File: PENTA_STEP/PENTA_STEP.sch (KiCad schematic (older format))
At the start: 154 parts, among them J1 DB25_Female_LCNC, J10 ENC_HEADER, J11 ENC_HEADER, J12 PSoC_PROG, J14 SCREW TERM, J15 SCREW TERM, J16 ENC_HEADER, J17 ENC_HEADER, J18 SCREW TERM, J19 SCREW TERM, J2 MTA-100, J20 CYP_I2C, J3 USB_B, J4 SPARE_IN, J5 ENC_HEADER, J6 Conn_02x02_Odd_Even, J7 CYP_GPIO, J8 ICSP, J9 SCREW TERM, U1 ATTINY841-SSU, U2 CY8C5468AXI-LP106, Y1 10MHz

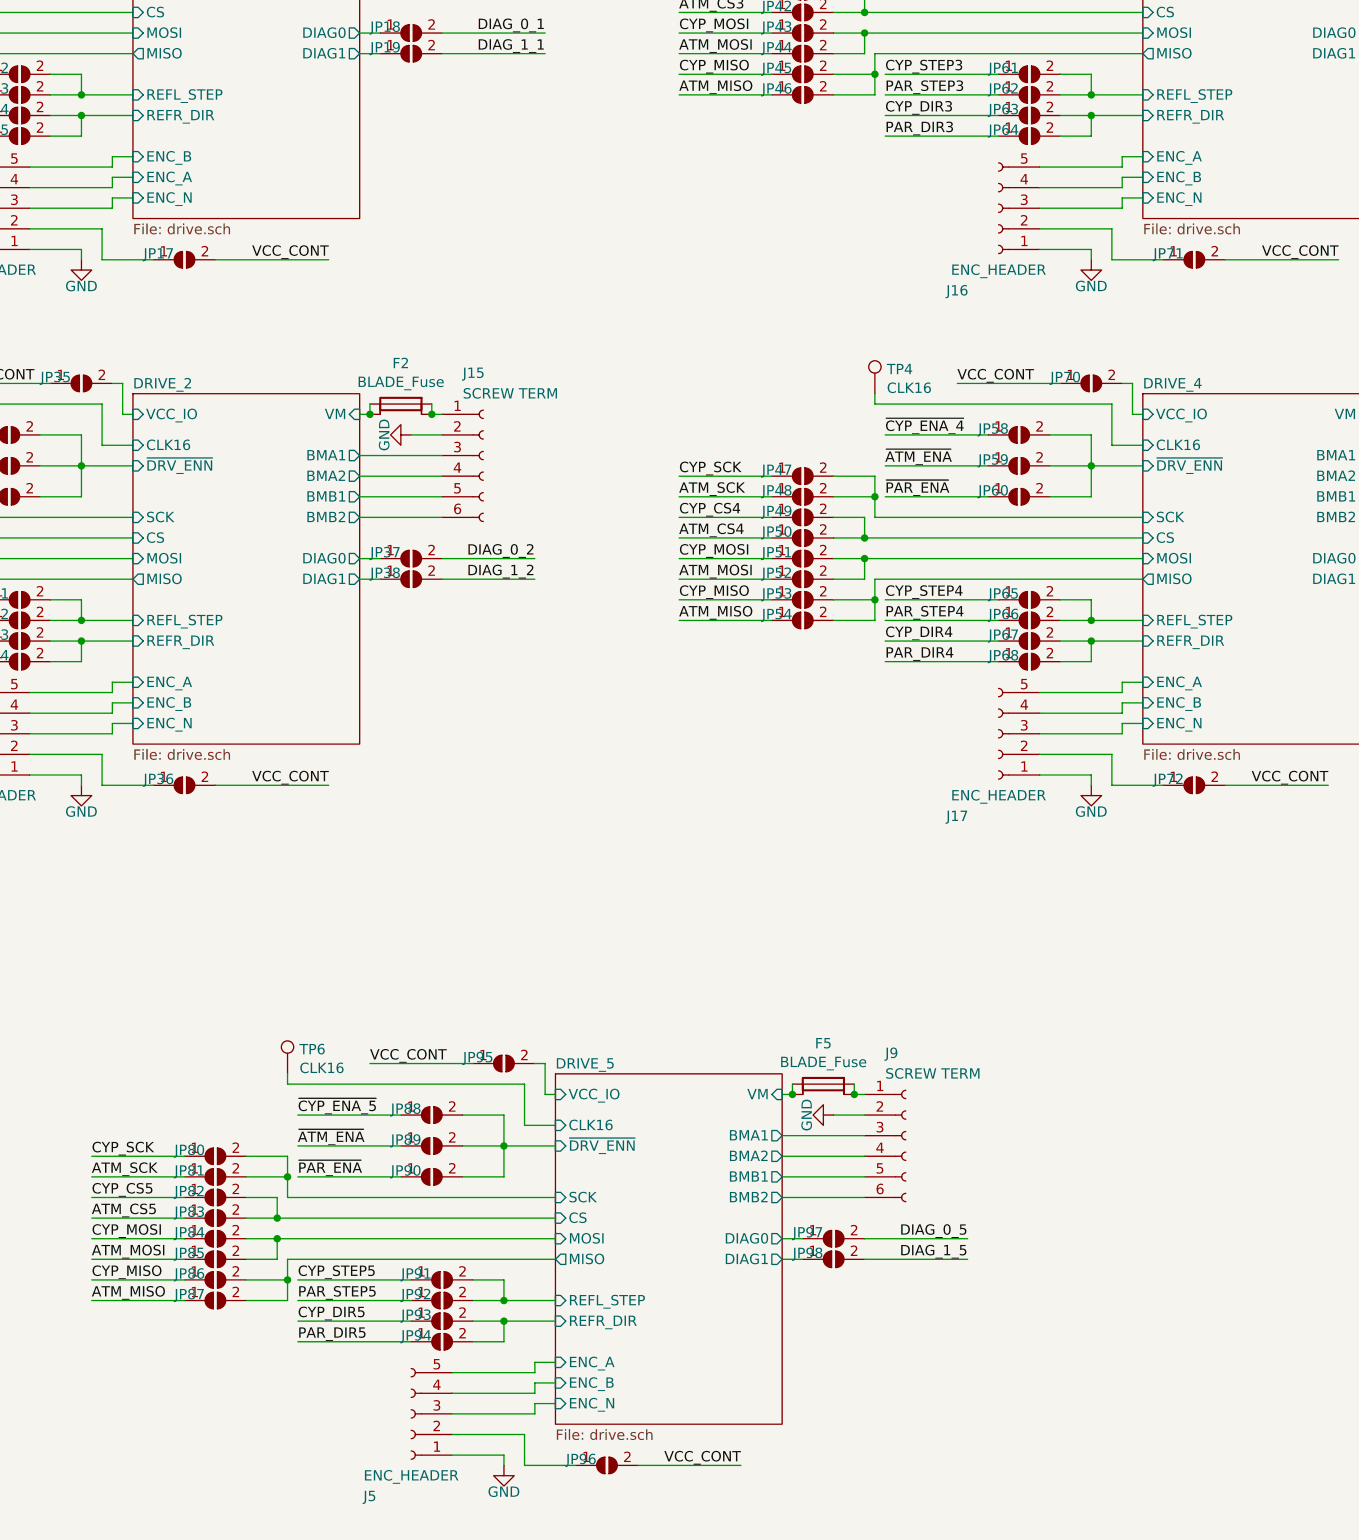
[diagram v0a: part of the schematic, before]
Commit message: corrected symbol and footprint paths
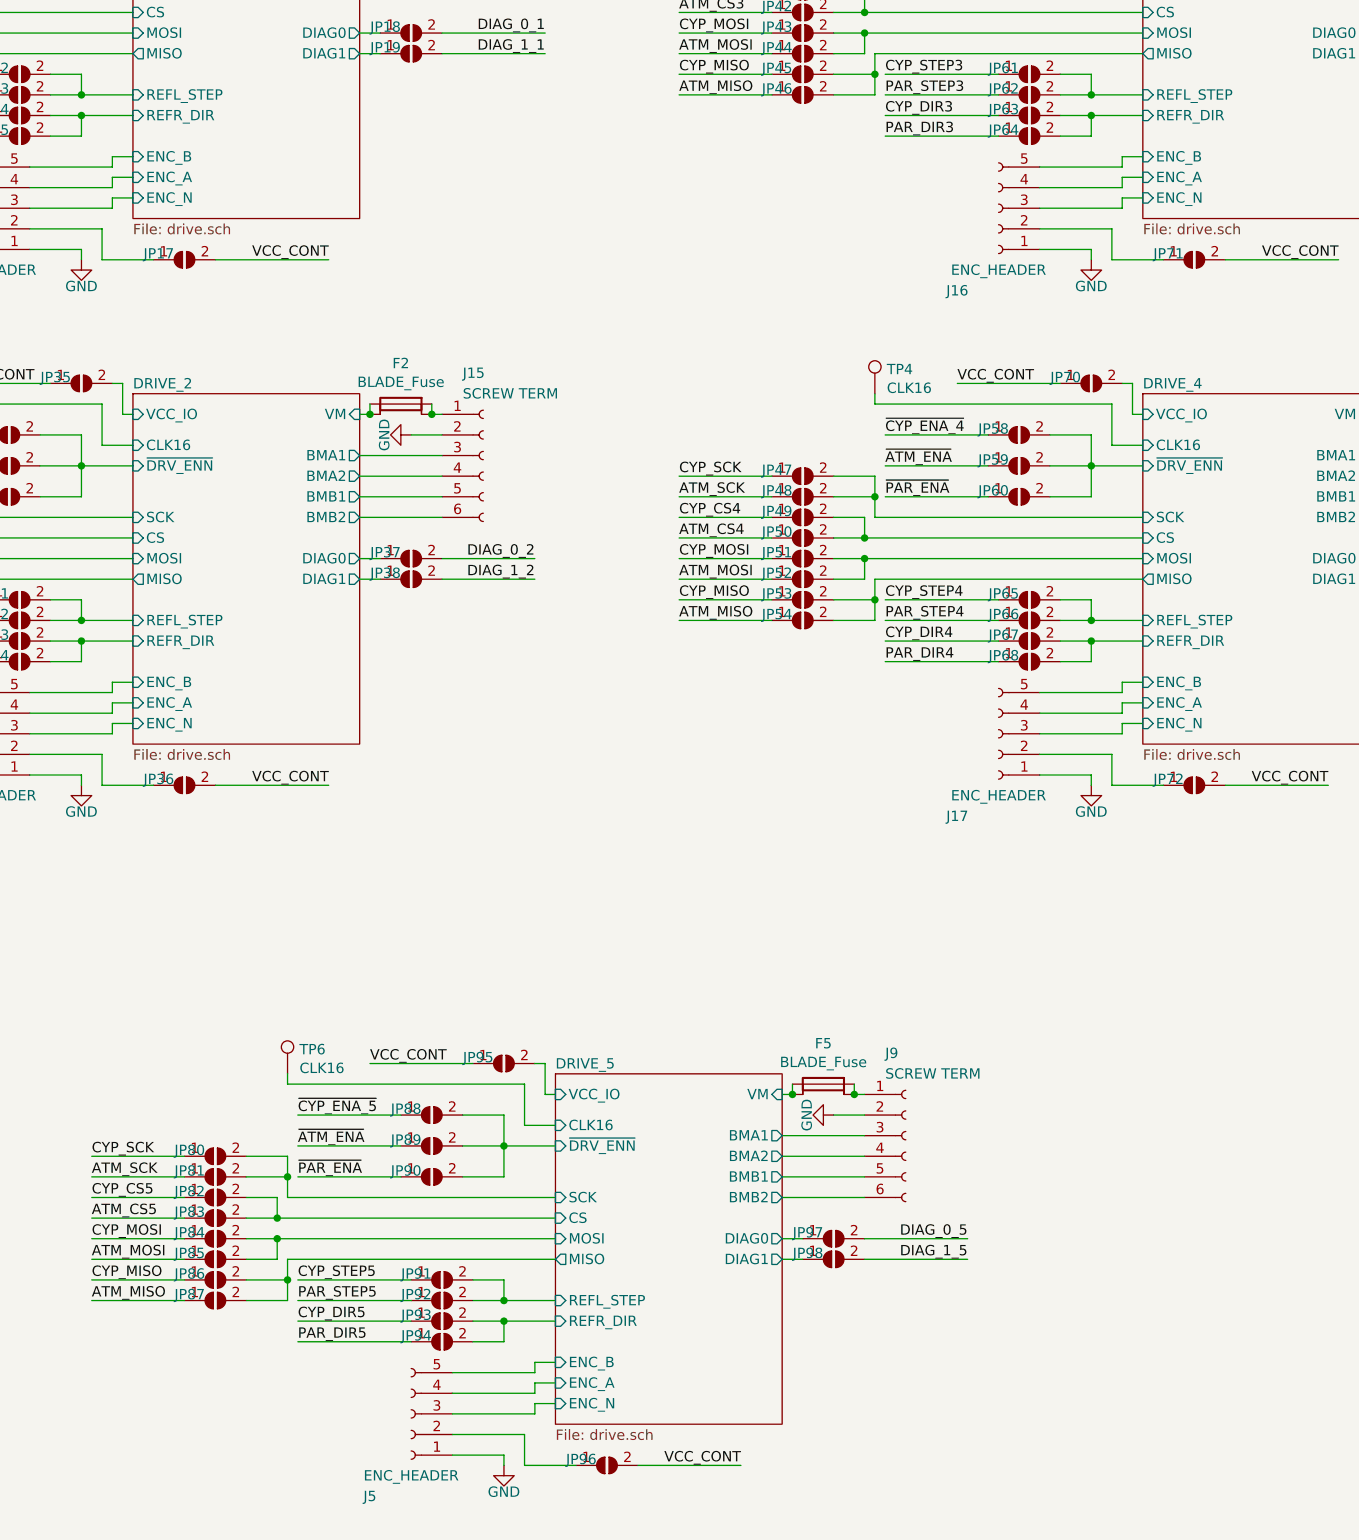
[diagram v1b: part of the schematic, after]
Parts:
- F1, F2, F3, F4: footprint CUSTOM:keystone_3549_2_fuseholder_THT -> CUSTOM_FP:keystone_3549_2_fuseholder_THT
- J1: footprint Connector_Dsub:DSUB-25_Female_Horizontal_P2.77x2.84mm_EdgePinOffset7.70mm_Housed_MountingHolesOffset9.12mm -> CUSTOM_FP:DSUB-25_Female_Horizontal_P2.77x2.84mm_EdgePinOffset7.70mm_Housed_MountingHolesOffset9.12mm
- J14, J15, J18, J19: footprint CUSTOM:CUI_TB002-500-06BE -> CUSTOM_FP:CUI_TB002-500-06BE
- J3: footprint CUSTOM:CUI_UJ2-BH-W1-TH -> CUSTOM_FP:CUI_UJ2-BH-W1-TH
- JP1, JP10, JP11, JP12, JP13, JP14, JP15, JP16, JP17, JP18, JP19, JP2, JP20, JP21, JP22, JP23, JP24, JP25, JP26, JP27, JP28, JP29, JP3, JP30, JP31, JP32, JP33, JP34, JP35, JP36, JP37, JP38, JP39, JP4, JP40, JP41, JP42, JP43, JP44, JP45, JP46, JP47, JP48, JP49, JP5, JP50, JP51, JP52, JP53, JP54, JP55, JP56, JP57, JP58, JP59, JP6, JP60, JP61, JP62, JP63, JP64, JP65, JP66, JP67, JP68, JP69, JP7, JP70, JP71, JP72, JP73, JP74, JP75, JP76, JP8, JP9: footprint CUSTOM:small_triangle_jumper -> CUSTOM_FP:small_triangle_jumper
- U1: footprint CUSTOM:ATTINY841-SSU -> CUSTOM_FP:ATTINY841-SSU
- U2: footprint CUSTOM:CY8C5468AXI-LP106 -> CUSTOM_FP:CY8C5468AXI-LP106
- Y1: footprint CUSTOM:CX5032GB10000H0PESZZ -> CUSTOM_FP:CX5032GB10000H0PESZZ
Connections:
- net DRIVE_2/ENC_A: now also J11.4 (Pin_4); no longer J11.5 (Pin_5)
- net DRIVE_2/ENC_B: now also J11.5 (Pin_5); no longer J11.4 (Pin_4)
- net DRIVE_3/ENC_A: now also J16.4 (Pin_4); no longer J16.5 (Pin_5)
- net DRIVE_3/ENC_B: now also J16.5 (Pin_5); no longer J16.4 (Pin_4)
- net DRIVE_4/ENC_A: now also J17.4 (Pin_4); no longer J17.5 (Pin_5)
- net DRIVE_4/ENC_B: now also J17.5 (Pin_5); no longer J17.4 (Pin_4)
- net DRIVE_5/ENC_A: now also J5.4 (Pin_4); no longer J5.5 (Pin_5)
- net DRIVE_5/ENC_B: now also J5.5 (Pin_5); no longer J5.4 (Pin_4)

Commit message: V1 layout nearing completion
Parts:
- C1, C10, C11, C12, C13, C14, C15, C2, C3, C4, C6, C8, C9: footprint Capacitor_SMD:C_0603_1608Metric -> Capacitor_SMD:C_0603_1608Metric_Pad1.05x0.95mm_HandSolder
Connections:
- net DRIVE_1/BMA1: now also J14.5 (Pin_5); no longer J14.3 (Pin_3)
- net DRIVE_1/BMA2: now also J14.6 (Pin_6); no longer J14.4 (Pin_4)
- net DRIVE_1/BMB1: now also J14.3 (Pin_3); no longer J14.5 (Pin_5)
- net DRIVE_1/BMB2: now also J14.4 (Pin_4); no longer J14.6 (Pin_6)
- net DRIVE_2/BMA1: now also J15.5 (Pin_5); no longer J15.3 (Pin_3)
- net DRIVE_2/BMA2: now also J15.6 (Pin_6); no longer J15.4 (Pin_4)
- net DRIVE_2/BMB1: now also J15.3 (Pin_3); no longer J15.5 (Pin_5)
- net DRIVE_2/BMB2: now also J15.4 (Pin_4); no longer J15.6 (Pin_6)
- net DRIVE_3/BMA1: now also J18.5 (Pin_5); no longer J18.3 (Pin_3)
- net DRIVE_3/BMA2: now also J18.6 (Pin_6); no longer J18.4 (Pin_4)
- net DRIVE_3/BMB1: now also J18.3 (Pin_3); no longer J18.5 (Pin_5)
- net DRIVE_3/BMB2: now also J18.4 (Pin_4); no longer J18.6 (Pin_6)
- net DRIVE_4/BMA1: now also J19.5 (Pin_5); no longer J19.3 (Pin_3)
- net DRIVE_4/BMA2: now also J19.6 (Pin_6); no longer J19.4 (Pin_4)
- net DRIVE_4/BMB1: now also J19.3 (Pin_3); no longer J19.5 (Pin_5)
- net DRIVE_4/BMB2: now also J19.4 (Pin_4); no longer J19.6 (Pin_6)
- net DRIVE_5/BMA1: now also J9.5 (Pin_5); no longer J9.3 (Pin_3)
- net DRIVE_5/BMA2: now also J9.6 (Pin_6); no longer J9.4 (Pin_4)
- net DRIVE_5/BMB1: now also J9.3 (Pin_3); no longer J9.5 (Pin_5)
- net DRIVE_5/BMB2: now also J9.4 (Pin_4); no longer J9.6 (Pin_6)
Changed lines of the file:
@@
 F 0 "C2" H 3865 4696 50  0000 L CNN
 F 1 "100n" H 3865 4605 50  0000 L CNN
-F 2 "Capacitor_SMD:C_0603_1608Metric" H 3788 4500 50  0001 C CNN
+F 2 "Capacitor_SMD:C_0603_1608Metric_Pad1.05x0.95mm_HandSolder" H 3788 4500 50  0001 C CNN
 F 3 "" H 3750 4650 50  0001 C CNN
 F 4 "06031C104KAT2A" H 3750 4650 50  0001 C CNN "MPN"
@@
 F 0 "C1" H 3515 4696 50  0000 L CNN
 F 1 "10u" H 3515 4605 50  0000 L CNN
-F 2 "Capacitor_SMD:C_0603_1608Metric" H 3438 4500 50  0001 C CNN
+F 2 "Capacitor_SMD:C_0603_1608Metric_Pad1.05x0.95mm_HandSolder" H 3438 4500 50  0001 C CNN
 F 3 "" H 3400 4650 50  0001 C CNN
 F 4 "JMK107ABJ106MA-T" H 3400 4650 50  0001 C CNN "MPN"
@@
 F1 "drive.sch" 50
 F2 "VM" I R 13400 2250 50
-F3 "BMA1" O R 13400 2450 50
-F4 "BMA2" O R 13400 2550 50
-F5 "BMB1" O R 13400 2650 50
-F6 "BMB2" O R 13400 2750 50
+F3 "BMA1" O R 13400 2650 50
+F4 "BMA2" O R 13400 2750 50
+F5 "BMB1" O R 13400 2450 50
+F6 "BMB2" O R 13400 2550 50
 F7 "CLK16" I L 12300 2400 50
 F8 "MISO" O L 12300 3050 50
@@
 F1 "drive.sch" 50
 F2 "VM" I R 13400 4800 50
-F3 "BMA1" O R 13400 5000 50
-F4 "BMA2" O R 13400 5100 50
-F5 "BMB1" O R 13400 5200 50
-F6 "BMB2" O R 13400 5300 50
+F3 "BMA1" O R 13400 5200 50
+F4 "BMA2" O R 13400 5300 50
+F5 "BMB1" O R 13400 5000 50
+F6 "BMB2" O R 13400 5100 50
 F7 "CLK16" I L 12300 4950 50
 F8 "~DRV_ENN" I L 12300 5050 50
@@
 F1 "drive.sch" 50
 F2 "VM" I R 18300 2250 50
-F3 "BMA1" O R 18300 2450 50
-F4 "BMA2" O R 18300 2550 50
-F5 "BMB1" O R 18300 2650 50
-F6 "BMB2" O R 18300 2750 50
+F3 "BMA1" O R 18300 2650 50
+F4 "BMA2" O R 18300 2750 50
+F5 "BMB1" O R 18300 2450 50
+F6 "BMB2" O R 18300 2550 50
 F7 "CLK16" I L 17200 2400 50
 F8 "~DRV_ENN" I L 17200 2500 50
@@
 F1 "drive.sch" 50
 F2 "VM" I R 18300 4800 50
-F3 "BMA1" O R 18300 5000 50
-F4 "BMA2" O R 18300 5100 50
-F5 "BMB1" O R 18300 5200 50
-F6 "BMB2" O R 18300 5300 50
+F3 "BMA1" O R 18300 5200 50
+F4 "BMA2" O R 18300 5300 50
+F5 "BMB1" O R 18300 5000 50
+F6 "BMB2" O R 18300 5100 50
 F7 "CLK16" I L 17200 4950 50
 F8 "~DRV_ENN" I L 17200 5050 50
@@
 F 0 "C8" H 6015 10396 50  0000 L CNN
 F 1 "100n" H 6015 10305 50  0000 L CNN
-F 2 "Capacitor_SMD:C_0603_1608Metric" H 5938 10200 50  0001 C CNN
+F 2 "Capacitor_SMD:C_0603_1608Metric_Pad1.05x0.95mm_HandSolder" H 5938 10200 50  0001 C CNN
 F 3 "" H 5900 10350 50  0001 C CNN
 F 4 "06031C104KAT2A" H 5900 10350 50  0001 C CNN "MPN"
@@
 F 0 "C9" H 6115 10846 50  0000 L CNN
 F 1 "100n" H 6115 10755 50  0000 L CNN
-F 2 "Capacitor_SMD:C_0603_1608Metric" H 6038 10650 50  0001 C CNN
+F 2 "Capacitor_SMD:C_0603_1608Metric_Pad1.05x0.95mm_HandSolder" H 6038 10650 50  0001 C CNN
 F 3 "" H 6000 10800 50  0001 C CNN
 F 4 "06031C104KAT2A" H 6000 10800 50  0001 C CNN "MPN"
@@
 F 0 "C10" H 6215 11296 50  0000 L CNN
 F 1 "100n" H 6215 11205 50  0000 L CNN
-F 2 "Capacitor_SMD:C_0603_1608Metric" H 6138 11100 50  0001 C CNN
+F 2 "Capacitor_SMD:C_0603_1608Metric_Pad1.05x0.95mm_HandSolder" H 6138 11100 50  0001 C CNN
 F 3 "" H 6100 11250 50  0001 C CNN
 F 4 "06031C104KAT2A" H 6100 11250 50  0001 C CNN "MPN"
@@
 F 0 "C11" H 6315 11746 50  0000 L CNN
 F 1 "100n" H 6315 11655 50  0000 L CNN
-F 2 "Capacitor_SMD:C_0603_1608Metric" H 6238 11550 50  0001 C CNN
+F 2 "Capacitor_SMD:C_0603_1608Metric_Pad1.05x0.95mm_HandSolder" H 6238 11550 50  0001 C CNN
 F 3 "" H 6200 11700 50  0001 C CNN
 F 4 "06031C104KAT2A" H 6200 11700 50  0001 C CNN "MPN"
@@
 F 0 "C15" H 6815 9396 50  0000 L CNN
 F 1 "100n" H 6815 9305 50  0000 L CNN
-F 2 "Capacitor_SMD:C_0603_1608Metric" H 6738 9200 50  0001 C CNN
+F 2 "Capacitor_SMD:C_0603_1608Metric_Pad1.05x0.95mm_HandSolder" H 6738 9200 50  0001 C CNN
 F 3 "" H 6700 9350 50  0001 C CNN
 F 4 "06031C104KAT2A" H 6700 9350 50  0001 C CNN "MPN"
@@
 F 0 "C13" H 6665 8796 50  0000 L CNN
 F 1 "100n" H 6665 8705 50  0000 L CNN
-F 2 "Capacitor_SMD:C_0603_1608Metric" H 6588 8600 50  0001 C CNN
+F 2 "Capacitor_SMD:C_0603_1608Metric_Pad1.05x0.95mm_HandSolder" H 6588 8600 50  0001 C CNN
 F 3 "" H 6550 8750 50  0001 C CNN
 F 4 "06031C104KAT2A" H 6550 8750 50  0001 C CNN "MPN"
@@
 F 0 "C14" H 6665 12846 50  0000 L CNN
 F 1 "100n" H 6665 12755 50  0000 L CNN
-F 2 "Capacitor_SMD:C_0603_1608Metric" H 6588 12650 50  0001 C CNN
+F 2 "Capacitor_SMD:C_0603_1608Metric_Pad1.05x0.95mm_HandSolder" H 6588 12650 50  0001 C CNN
 F 3 "" H 6550 12800 50  0001 C CNN
 F 4 "06031C104KAT2A" H 6550 12800 50  0001 C CNN "MPN"
@@
 F 0 "C12" H 6415 12446 50  0000 L CNN
 F 1 "1u" H 6415 12355 50  0000 L CNN
-F 2 "Capacitor_SMD:C_0603_1608Metric" H 6338 12250 50  0001 C CNN
+F 2 "Capacitor_SMD:C_0603_1608Metric_Pad1.05x0.95mm_HandSolder" H 6338 12250 50  0001 C CNN
 F 3 "" H 6300 12400 50  0001 C CNN
 F 4 "CL10B105MO8NNWC" H 6300 12400 50  0001 C CNN "MPN"
@@
 F 0 "C4" H 4865 11746 50  0000 L CNN
 F 1 "1u" H 4865 11655 50  0000 L CNN
-F 2 "Capacitor_SMD:C_0603_1608Metric" H 4788 11550 50  0001 C CNN
+F 2 "Capacitor_SMD:C_0603_1608Metric_Pad1.05x0.95mm_HandSolder" H 4788 11550 50  0001 C CNN
 F 3 "" H 4750 11700 50  0001 C CNN
 F 4 "CL10B105MO8NNWC" H 4750 11700 50  0001 C CNN "MPN"
@@
 F 0 "C6" H 5315 11746 50  0000 L CNN
 F 1 "1u" H 5315 11655 50  0000 L CNN
-F 2 "Capacitor_SMD:C_0603_1608Metric" H 5238 11550 50  0001 C CNN
+F 2 "Capacitor_SMD:C_0603_1608Metric_Pad1.05x0.95mm_HandSolder" H 5238 11550 50  0001 C CNN
 F 3 "" H 5200 11700 50  0001 C CNN
 F 4 "CL10B105MO8NNWC" H 5200 11700 50  0001 C CNN "MPN"
@@
 F 0 "C3" H 4415 11746 50  0000 L CNN
 F 1 "1u" H 4415 11655 50  0000 L CNN
-F 2 "Capacitor_SMD:C_0603_1608Metric" H 4338 11550 50  0001 C CNN
+F 2 "Capacitor_SMD:C_0603_1608Metric_Pad1.05x0.95mm_HandSolder" H 4338 11550 50  0001 C CNN
 F 3 "" H 4300 11700 50  0001 C CNN
 F 4 "CL10B105MO8NNWC" H 4300 11700 50  0001 C CNN "MPN"
@@
 F1 "drive.sch" 50
 F2 "VM" I R 15450 8100 50
-F3 "BMA1" O R 15450 8300 50
-F4 "BMA2" O R 15450 8400 50
-F5 "BMB1" O R 15450 8500 50
-F6 "BMB2" O R 15450 8600 50
+F3 "BMA1" O R 15450 8500 50
+F4 "BMA2" O R 15450 8600 50
+F5 "BMB1" O R 15450 8300 50
+F6 "BMB2" O R 15450 8400 50
 F7 "CLK16" I L 14350 8250 50
 F8 "~DRV_ENN" I L 14350 8350 50

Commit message: Added two FET-controlled outputs to the board
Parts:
- added J13: PWR_SW_CH1, CUSTOM_FP:1776275-4, symbol Connector:Conn_01x04_Female
- added J21: PWR_SW_CH2, CUSTOM_FP:1776275-4, symbol Connector:Conn_01x04_Female
- added Q21: AON7804, CUSTOM_FP:DFN3X3_AON7804, symbol AON7804:AON7804
- added R1, R2: 2R2, Resistor_SMD:R_0603_1608Metric_Pad1.05x0.95mm_HandSolder, symbol Device:R
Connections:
- net CYP_CS1: now also U2.9 (P67); no longer U2.99 (P24)
- net CYP_DIR1: now also U2.7 (P65); no longer U2.84 (P46)
- net CYP_STEP1: now also U2.8 (P66); no longer U2.85 (P47)
- net GND: now also J13.2 (Pin_2), J21.2 (Pin_2), Q21.S1 (S), Q21.S2 (S)
- net PAR_DIR1: now also J1.8; no longer J1.3
- net PAR_DIR2: now also J1.6; no longer J1.5
- net PAR_DIR3: now also J1.4; no longer J1.7
- net PAR_DIR4: now also J1.3; no longer J1.9
- net PAR_DIR5: now also J1.14 (P14); no longer J1.16 (P16)
- net PAR_STEP1: now also J1.9; no longer J1.2
- net PAR_STEP2: now also J1.7; no longer J1.4
- net PAR_STEP3: now also J1.5; no longer J1.6
- net PAR_STEP4: now also J1.16 (P16); no longer J1.8
- net PAR_STEP5: now also J1.2; no longer J1.14 (P14)
- net at J7.1 (Pin_1): now also U2.34 (P57); no longer U2.22 (P12)
- net at J7.10 (Pin_10): now also U2.27 (P16); no longer U2.34 (P57)
- net at J7.2 (Pin_2): now also U2.22 (P12); no longer U2.23 (P13)
- net at J7.3 (Pin_3): now also U2.33 (P56); no longer U2.24 (P14)
- net at J7.4 (Pin_4): now also U2.23 (P13); no longer U2.25 (P15)
- net at J7.5 (Pin_5): now also U2.32 (P55); no longer U2.27 (P16)
- net at J7.6 (Pin_6): now also U2.24 (P14); no longer U2.28 (P17)
- net at J7.8 (Pin_8): now also U2.25 (P15); no longer U2.32 (P55)
- net at J7.9 (Pin_9): now also U2.28 (P17); no longer U2.33 (P56)
- new net: J13.1 (Pin_1), J13.3 (Pin_3)
- new net: J13.4 (Pin_4), Q21.D1 (D), Q21.D1A (D1)
- new net: J21.1 (Pin_1), J21.3 (Pin_3)
- new net: J21.4 (Pin_4), Q21.D2 (D), Q21.D2A (D1)
- new net: Q21.G1 (G), R1.1
- new net: Q21.G2 (G), R2.1
- new net PWR_SW_CH1: R1.2, U2.85 (P47)
- new net PWR_SW_CH2: R2.2, U2.84 (P46)
- no-connect marks 24 -> 22
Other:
- moved on the sheet: J20, J7, R162, R163
